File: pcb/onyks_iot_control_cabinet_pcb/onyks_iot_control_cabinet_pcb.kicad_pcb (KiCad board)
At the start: 2 copper layers, 80 x 90 mm, 38 parts, among them J1 Conn_01x02_Socket, J10 Conn_02x05_Odd_Even, J2 Conn_01x06_Socket, J3 Screw_Terminal_01x02, J4 Jack-DC, J5 Conn_01x03_Pin, J6 Conn_02x09_Odd_Even, J7 Screw_Terminal_01x02, J8 Conn_01x06_Pin, J9 Conn_01x02_Socket, Q1 SQ4050EY-T1_GE3, Q2 SQ4050EY-T1_GE3, Q3 NPN, Q4 NPN, SW1 SW_Push, SW2 SW_Push, SW3 SW_Push, U1 ESP32-WROOM-32D, U2 LMR51430

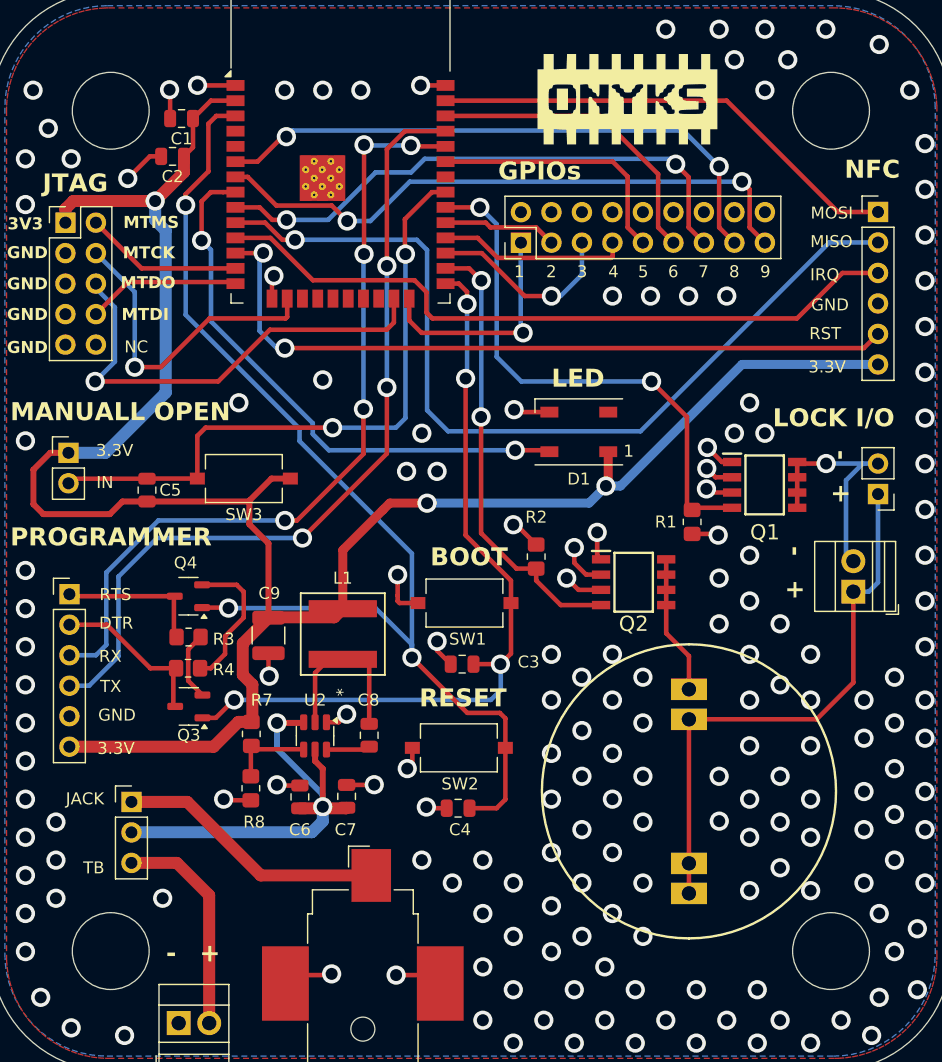
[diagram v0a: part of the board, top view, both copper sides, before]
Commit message: Karol can't add mounting holes/Added
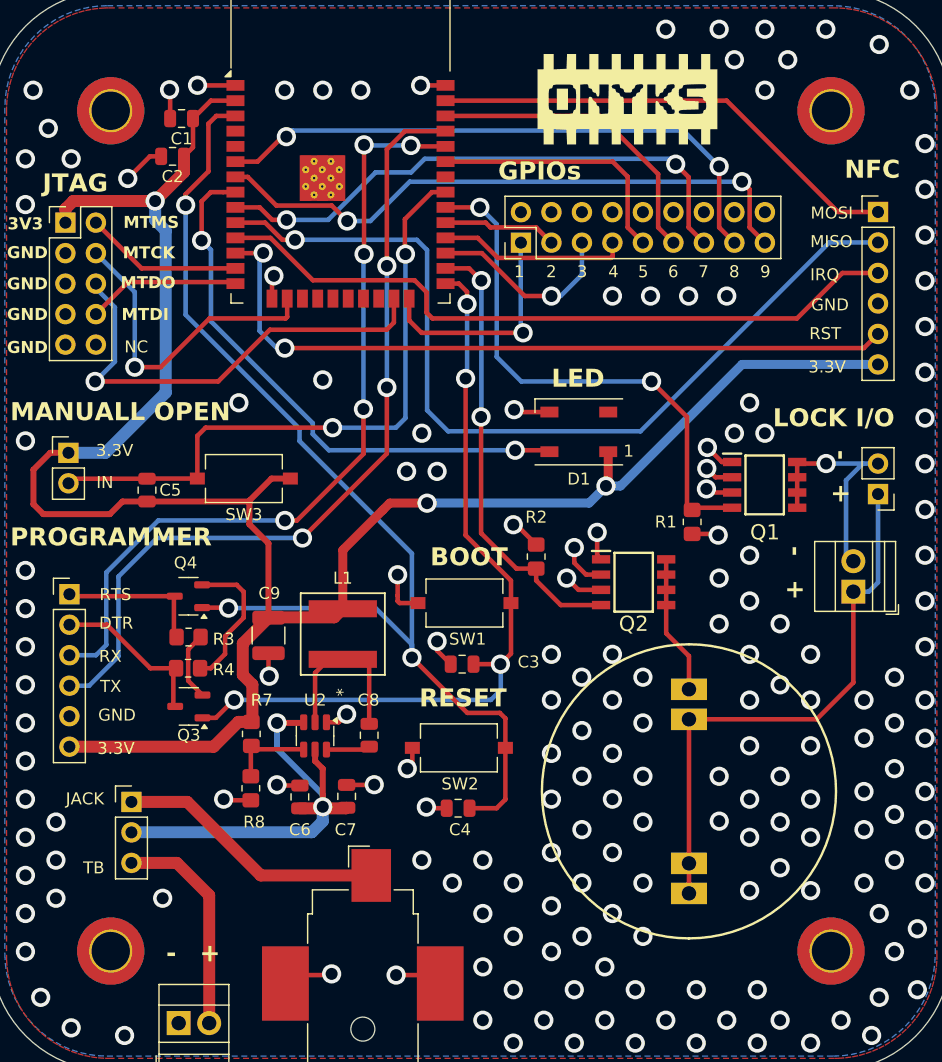
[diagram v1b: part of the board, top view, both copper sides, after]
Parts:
- added H1: MountingHole_Pad, MountingHole:MountingHole_3.2mm_M3_DIN965_Pad_TopBottom, F.Cu at (116.0, 36.0)
- added H2: MountingHole_Pad, MountingHole:MountingHole_3.2mm_M3_DIN965_Pad_TopBottom, F.Cu at (116.0, 106.0)
- added H3: MountingHole_Pad, MountingHole:MountingHole_3.2mm_M3_DIN965_Pad_TopBottom, F.Cu at (56.0, 36.0)
- added H4: MountingHole_Pad, MountingHole:MountingHole_3.2mm_M3_DIN965_Pad_TopBottom, F.Cu at (56.0, 106.0)
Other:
- outline, holes or cut-outs redrawn

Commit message: PCB Update for package
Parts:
- removed J9: Conn_01x02_Socket, Connector_PinHeader_2.54mm:PinHeader_1x02_P2.54mm_Vertical
- moved J3 25.3 mm to (87.0, 111.1)
- moved R2 10.2 mm to (101.6, 72.4)
- moved Q2 9.10 mm to (108.0, 71.8)
- moved R1 7.54 mm to (110.5, 65.8), turned to 90 degrees
- moved Q1 6.61 mm to (116.8, 65.4)
- moved J4 5.98 mm to (71.1, 104.4)
- moved J7 5.63 mm to (121.1, 80.6)
- moved BZ1 3.16 mm to (104.2, 83.5)
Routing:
- net GND: track 66.9 -> 37.2 mm, vias 180 -> 164
- net Net-(J3-Pin_2): track 18.2 -> 37.7 mm
- net LOCK_PLUS: track 46.8 -> 32.7 mm
- net BUZZER_SWITCH: track 37.5 -> 43.9 mm
- net Net-(J5-Pin_1): track 22.5 -> 16.2 mm
- net LOCK_MINUS: track 19.6 -> 15.3 mm, vias 1 -> 0
- net Net-(BZ1--_2): track 11.6 -> 15.0 mm
- net LOCK_SWITCH: track 45.1 -> 47.4 mm

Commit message: PCB Overhaul
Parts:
- removed C8: 0.1u, Capacitor_SMD:C_0805_2012Metric
- removed C9: 100u, Capacitor_SMD:C_1210_3225Metric
- removed G***: LOGO, ourFootprints:LOGO
- removed J8: Conn_01x06_Pin, Connector_PinHeader_2.54mm:PinHeader_1x06_P2.54mm_Vertical
- removed Q4: NPN, Package_TO_SOT_SMD:SOT-23-3
- removed R7: 100k, Resistor_SMD:R_0805_2012Metric_Pad1.20x1.40mm_HandSolder
- removed R8: 22.1k, Resistor_SMD:R_0805_2012Metric_Pad1.20x1.40mm_HandSolder
- added C10: 22u/10V, Capacitor_SMD:C_0603_1608Metric, F.Cu at (176.5, 53.3)
- added C11: 0.1u/50V, Capacitor_SMD:C_0603_1608Metric, F.Cu at (174.6, 53.3)
- added D2: S5J, Diode_SMD:D_SMC, F.Cu at (211.5, 82.5)
- added D3: S5J, Diode_SMD:D_SMC, F.Cu at (188.0, 100.6)
- added J9: Conn_02x05_Odd_Even, Connector_PinHeader_2.54mm:PinHeader_2x05_P2.54mm_Vertical, F.Cu at (164.1, 84.8)
- added Q5: PMV100ENEAR, Package_TO_SOT_SMD:SOT-23, F.Cu at (204.3, 82.9)
- added R5: 100k, Resistor_SMD:R_0805_2012Metric_Pad1.20x1.40mm_HandSolder, F.Cu at (180.8, 97.2)
- added R6: 22.1k, Resistor_SMD:R_0805_2012Metric_Pad1.20x1.40mm_HandSolder, F.Cu at (181.9, 92.5)
- BZ1: value Buzzer -> CPI2416100T
- C1: value 22u -> 0.1u/50V; footprint Capacitor_SMD:C_0805_2012Metric -> Capacitor_SMD:C_0603_1608Metric
- C2, C3: value 0.1u -> 0.1u/50V; footprint Capacitor_SMD:C_0805_2012Metric -> Capacitor_SMD:C_0603_1608Metric
- C4: value 0.1u -> 2.2u/50V; footprint Capacitor_SMD:C_0805_2012Metric -> Capacitor_SMD:C_0603_1608Metric
- C5: value 0.1u -> 100n/50V; footprint Capacitor_SMD:C_0805_2012Metric -> Capacitor_SMD:C_0603_1608Metric
- C6: value 2.2u -> 100n/50V
- C7: value 100n -> 100u/6.3V; footprint Capacitor_SMD:C_0805_2012Metric -> Capacitor_SMD:C_1210_3225Metric
- J1: value Conn_01x02_Socket -> Screw_Terminal_01x02; footprint Connector_PinHeader_2.54mm:PinHeader_1x02_P2.54mm_Vertical -> TerminalBlock:TerminalBlock_Xinya_XY308-2.54-2P_1x02_P2.54mm_Horizontal
- J10: value Conn_02x05_Odd_Even -> Conn_01x06_Pin; footprint Connector_PinHeader_2.54mm:PinHeader_2x05_P2.54mm_Vertical -> Connector_PinHeader_2.54mm:PinHeader_1x06_P2.54mm_Vertical
- J2: value Conn_01x06_Socket -> Screw_Terminal_01x02; footprint Connector_PinHeader_2.54mm:PinHeader_1x06_P2.54mm_Vertical -> TerminalBlock:TerminalBlock_Xinya_XY308-2.54-2P_1x02_P2.54mm_Horizontal
- J3: value Screw_Terminal_01x02 -> Jack-DC; footprint TerminalBlock:TerminalBlock_Xinya_XY308-2.54-2P_1x02_P2.54mm_Horizontal -> Connector_BarrelJack:BarrelJack_CUI_PJ-036AH-SMT_Horizontal
- J4: value Jack-DC -> Conn_01x03_Pin; footprint Connector_BarrelJack:BarrelJack_CUI_PJ-036AH-SMT_Horizontal -> Connector_PinHeader_2.54mm:PinHeader_1x03_P2.54mm_Vertical
- J5: value Conn_01x03_Pin -> Conn_02x09_Odd_Even; footprint Connector_PinHeader_2.54mm:PinHeader_1x03_P2.54mm_Vertical -> Connector_PinHeader_2.54mm:PinHeader_2x09_P2.54mm_Vertical
- J6: value Conn_02x09_Odd_Even -> Conn_01x06_Socket; footprint Connector_PinHeader_2.54mm:PinHeader_2x09_P2.54mm_Vertical -> Connector_PinHeader_2.54mm:PinHeader_1x06_P2.54mm_Vertical
- J7: value Screw_Terminal_01x02 -> Conn_01x02_Socket; footprint TerminalBlock:TerminalBlock_Xinya_XY308-2.54-2P_1x02_P2.54mm_Horizontal -> Connector_PinHeader_2.54mm:PinHeader_1x02_P2.54mm_Vertical
- L1: value 5.6u -> XAL6060-562MEC_COC
- Q1, Q2: value SQ4050EY-T1_GE3 -> NPN; footprint ourFootprints:SOIC127P600X175-8N -> Package_TO_SOT_SMD:SOT-23-3
- Q3: value NPN -> PMV100ENEAR; footprint Package_TO_SOT_SMD:SOT-23-3 -> Package_TO_SOT_SMD:SOT-23
- R1, R2: value 100 -> 10k
- R3, R4: value 10k -> 100
- U2: value LMR51430 -> LMR51430XDDCR
- moved H3 184.7 mm to (220.5, 120.1)
- moved J5 158.2 mm to (211.1, 54.9)
- moved J1 143.8 mm to (186.0, 118.1)
- moved R4 143.1 mm to (205.1, 93.4), turned to -90 degrees
- moved Q3 139.6 mm to (201.9, 93.4), turned to -90 degrees
- moved R3 138.8 mm to (201.2, 82.8), turned to 90 degrees
- moved J6 132.4 mm to (222.0, 59.4), turned to 0 degrees
- moved SW1 131.8 mm to (216.5, 90.8), turned to -90 degrees
- moved C3 127.1 mm to (212.1, 90.9), turned to -90 degrees
- moved C5 118.9 mm to (174.6, 95.2), turned to 180 degrees
- moved J10 117.7 mm to (161.5, 88.9), turned to 90 degrees
- moved U1 114.4 mm to (188.1, 60.4)
- moved C1 113.6 mm to (170.8, 69.0), turned to -90 degrees
- moved C7 111.9 mm to (187.5, 87.6), turned to -90 degrees
- moved J2 107.5 mm to (220.0, 83.8), turned to 90 degrees
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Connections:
- net Net-(D1-DIN) renamed /MCU/GPIO_32
- BZ1 pad A1: LOCK_PLUS -> +12V
- BZ1 pad B1: LOCK_PLUS -> +12V
- BZ1 pad B2: LOCK_PLUS -> +12V
- C1 pad 1: +3.3V -> /MCU/MCU_BOOT
- C2 pad 1: +3.3V -> /MCU/MCU_RESET
- C3 pad 1: GND -> +3.3V
- C3 pad 2: MCU_BOOT -> /MCU/GPIO_19
- C4 pad 1: GND -> +12V
- C4 pad 2: MCU_RESET -> GND
- C5 pad 1: +3.3V -> +12V
- C5 pad 2: LOCK_MCU_MANUAL_OPEN -> GND
- C6 pad 1: V_IN -> Net-(U2-CB)
- C6 pad 2: GND -> Net-(U2-SW)
- C7 pad 1: V_IN -> +3.3V
- J1 pad 1: +3.3V -> GND
- J1 pad 2: LOCK_MCU_MANUAL_OPEN -> Net-(J1-Pin_2)
- J10 pad 1: +3.3V -> /MCU/RTS
- J10 pad 2: JTAG_MTMS -> /MCU/DTR
- J10 pad 3: GND -> /MCU/RXD
- J10 pad 4: JTAG_MTCK -> /MCU/TXD
- J10 pad 6: JTAG_MTDO -> +3.3V
- J2 pad 1: NFC_MOSI -> +12V
- J2 pad 2: NFC_MISO -> Net-(D2-A)
- J3 pad 1: GND -> Net-(J4-Pin_1)
- J3 pad 2: Net-(J3-Pin_2) -> GND
- J4 pad 1: Net-(J5-Pin_1) -> Net-(J4-Pin_1)
- J4 pad 2: GND -> +12V
- J4 pad 3: GND -> Net-(J1-Pin_2)
- J5 pad 1: Net-(J5-Pin_1) -> /MCU/GPIO_2
- J5 pad 2: V_IN -> GND
- J5 pad 3: Net-(J3-Pin_2) -> /MCU/GPIO_5
- J6 pad 1: FREE_GPIO_1 -> /MCU/GPIO_23
- J6 pad 2: GND -> /MCU/GPIO_25
- J6 pad 3: FREE_GPIO_2 -> /MCU/GPIO_26
- J6 pad 5: FREE_GPIO_3 -> /MCU/GPIO_27
- J6 pad 6: GND -> +3.3V
- J7 pad 1: LOCK_PLUS -> +3.3V
- J7 pad 2: LOCK_MINUS -> /MCU/GPIO_19
- Q1 pad 1: GND -> /MCU/MCU_BOOT
- Q1 pad 2: GND -> Net-(Q1-B)
- Q1 pad 3: GND -> /MCU/DTR
- Q2 pad 1: GND -> /MCU/MCU_RESET
- Q2 pad 2: GND -> Net-(Q2-B)
- Q2 pad 3: GND -> /MCU/RTS
- Q3 pad 1: MCU_BOOT -> /MCU/GPIO_4
- Q3 pad 2: Net-(Q3-B) -> GND
- Q3 pad 3: DTR -> Net-(BZ1--_2)
- R1 pad 1: LOCK_SWITCH -> Net-(Q1-B)
- R1 pad 2: GND -> /MCU/RTS
- R2 pad 1: BUZZER_SWITCH -> Net-(Q2-B)
- R2 pad 2: GND -> /MCU/DTR
- R3 pad 1: Net-(Q3-B) -> /MCU/GPIO_18
- R3 pad 2: RTS -> GND
- R4 pad 1: Net-(Q4-B) -> /MCU/GPIO_4
- R4 pad 2: DTR -> GND
- SW1 pad 1: GND -> +3.3V
- SW1 pad 2: MCU_BOOT -> /MCU/GPIO_19
- SW2 pad 1: GND -> /MCU/MCU_BOOT
- SW2 pad 2: MCU_RESET -> GND
- SW3 pad 1: +3.3V -> /MCU/MCU_RESET
- SW3 pad 2: LOCK_MCU_MANUAL_OPEN -> GND
- U1 pad 10: NFC_MISO -> /MCU/GPIO_25
- U1 pad 11: NFC_IRQ -> /MCU/GPIO_26
- U1 pad 12: NFC_RST -> /MCU/GPIO_27
- U1 pad 13: JTAG_MTMS -> /MCU/MTMS
- U1 pad 14: JTAG_MTDI -> /MCU/MTDI
- U1 pad 16: JTAG_MTCK -> /MCU/MTCK
- U1 pad 23: JTAG_MTDO -> /MCU/MTDO
- U1 pad 24: FREE_GPIO_1 -> /MCU/GPIO_2
- U1 pad 25: MCU_BOOT -> /MCU/MCU_BOOT
- U1 pad 26: BUZZER_SWITCH -> /MCU/GPIO_4
- U1 pad 27: FREE_GPIO_3 -> /MCU/GPIO_16
- U1 pad 28: FREE_GPIO_4 -> /MCU/GPIO_17
- U1 pad 29: FREE_GPIO_2 -> /MCU/GPIO_5
- U1 pad 3: MCU_RESET -> /MCU/MCU_RESET
- U1 pad 30: LOCK_SWITCH -> /MCU/GPIO_18
- U1 pad 31: LOCK_MCU_MANUAL_OPEN -> /MCU/GPIO_19
- U1 pad 33: FREE_GPIO_5 -> /MCU/GPIO_21
- U1 pad 34: MCU_RX_PROG -> /MCU/RXD
- U1 pad 35: MCU_TX_PROG -> /MCU/TXD
- U1 pad 36: FREE_GPIO_6 -> /MCU/GPIO_22
- U1 pad 37: NFC_MOSI -> /MCU/GPIO_23
- U1 pad 6: FREE_GPIO_8 -> /MCU/GPIO_34
- U1 pad 7: FREE_GPIO_9 -> /MCU/GPIO_35
- U1 pad 9: FREE_GPIO_7 -> /MCU/GPIO_33
- U2 pad 3: V_IN -> +12V
- U2 pad 5: V_IN -> +12V
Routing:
- net MCU_RESET: track 95.5 -> 0.00 mm, vias 3 -> 0
- net /MCU/GPIO_25: track 0.00 -> 77.0 mm, vias 0 -> 1
- net /MCU/GPIO_26: track 0.00 -> 75.6 mm, vias 0 -> 1
- net NFC_MISO: track 75.1 -> 0.00 mm, vias 1 -> 0
- net /MCU/RXD: track 0.00 -> 73.9 mm, vias 0 -> 1
- net /MCU/GPIO_27: track 0.00 -> 69.6 mm, vias 0 -> 1
- net MCU_TX_PROG: track 69.2 -> 0.00 mm, vias 3 -> 0
- net /MCU/TXD: track 0.00 -> 68.9 mm, vias 0 -> 1
- net MCU_RX_PROG: track 67.6 -> 0.00 mm, vias 5 -> 0
- net MCU_BOOT: track 65.3 -> 0.00 mm, vias 4 -> 0
- net /MCU/GPIO_19: track 0.00 -> 63.4 mm, vias 0 -> 2
- net NFC_RST: track 61.5 -> 0.00 mm, vias 2 -> 0
- net /MCU/MCU_BOOT: track 0.00 -> 60.6 mm, vias 0 -> 2
- net /MCU/GPIO_33: track 0.00 -> 60.5 mm, vias 0 -> 3
- net /MCU/GPIO_35: track 0.00 -> 58.9 mm, vias 0 -> 2
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- added copper zone on B.Cu, net +12V
- added copper zone on B.Cu, net Net-(J1-Pin_2)
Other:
- board size 80 x 90 mm -> 68.3 x 79.2 mm
- board text removed: "+"
- board text removed: "-"
- board text removed: "1"
- board text removed: "2"
- board text removed: "3"
- board text removed: "3.3V"
- board text removed: "3V3"
- board text removed: "4"
- board text removed: "5"
- board text removed: "6"
- board text removed: "7"
- board text removed: "8"
- board text removed: "9"
- board text removed: "BOOT"
- board text removed: "DTR"
- board text removed: "GND"
- board text removed: "GPIOs"
- board text removed: "IN"
- board text removed: "IRQ"
- board text removed: "JACK"
- board text removed: "JTAG"
- board text removed: "LED"
- board text removed: "LOCK I/O"
- board text removed: "MANUALL OPEN"
- board text removed: "MISO"
- board text removed: "MOSI"
- board text removed: "MTCK"
- board text removed: "MTDI"
- board text removed: "MTDO"
- board text removed: "MTMS"
- board text removed: "NC"
- board text removed: "NFC"
- board text removed: "PROGRAMMER"
- board text removed: "RESET"
- board text removed: "RST"
- board text removed: "RTS"
- board text removed: "RX"
- board text removed: "TB"
- board text removed: "TX"

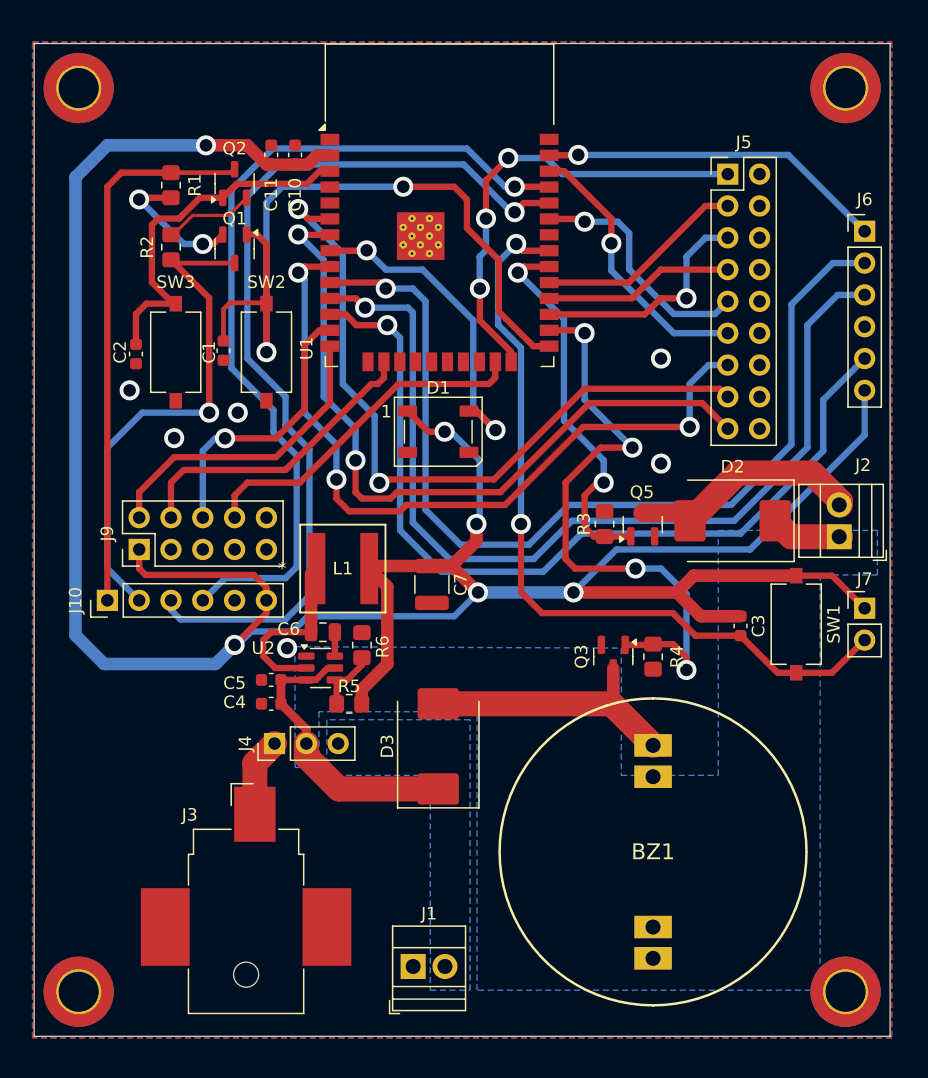
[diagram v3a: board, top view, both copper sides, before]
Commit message: Round corners and the logo
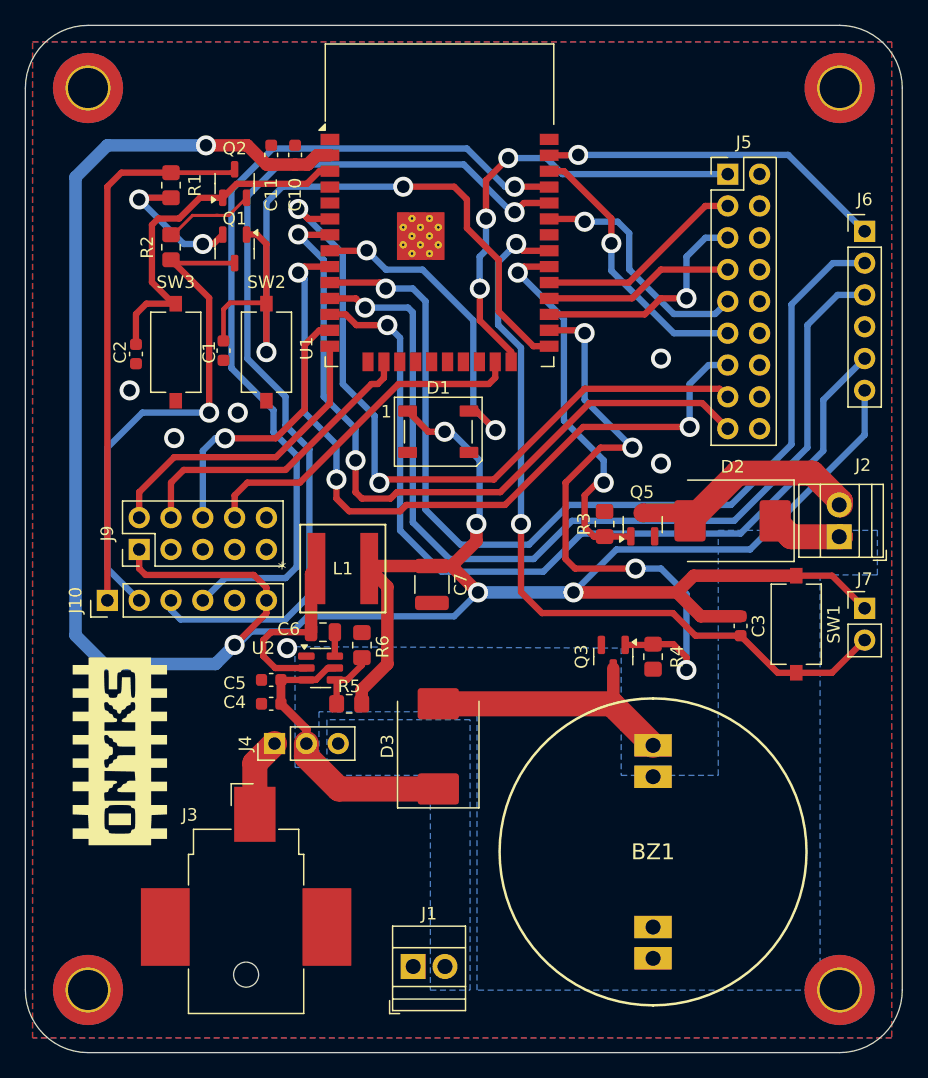
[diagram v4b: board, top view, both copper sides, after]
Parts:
- added G***: LOGO, ourFootprints:LOGO, F.Cu at (162.5, 101.0)
- moved H4 0.76 mm to (160.0, 120.0)
- moved H2 0.74 mm to (160.0, 48.0)
- moved H3 0.49 mm to (220.0, 120.0)
- moved H1 0.47 mm to (220.0, 48.0)
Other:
- board size 68.3 x 79.2 mm -> 70 x 82 mm

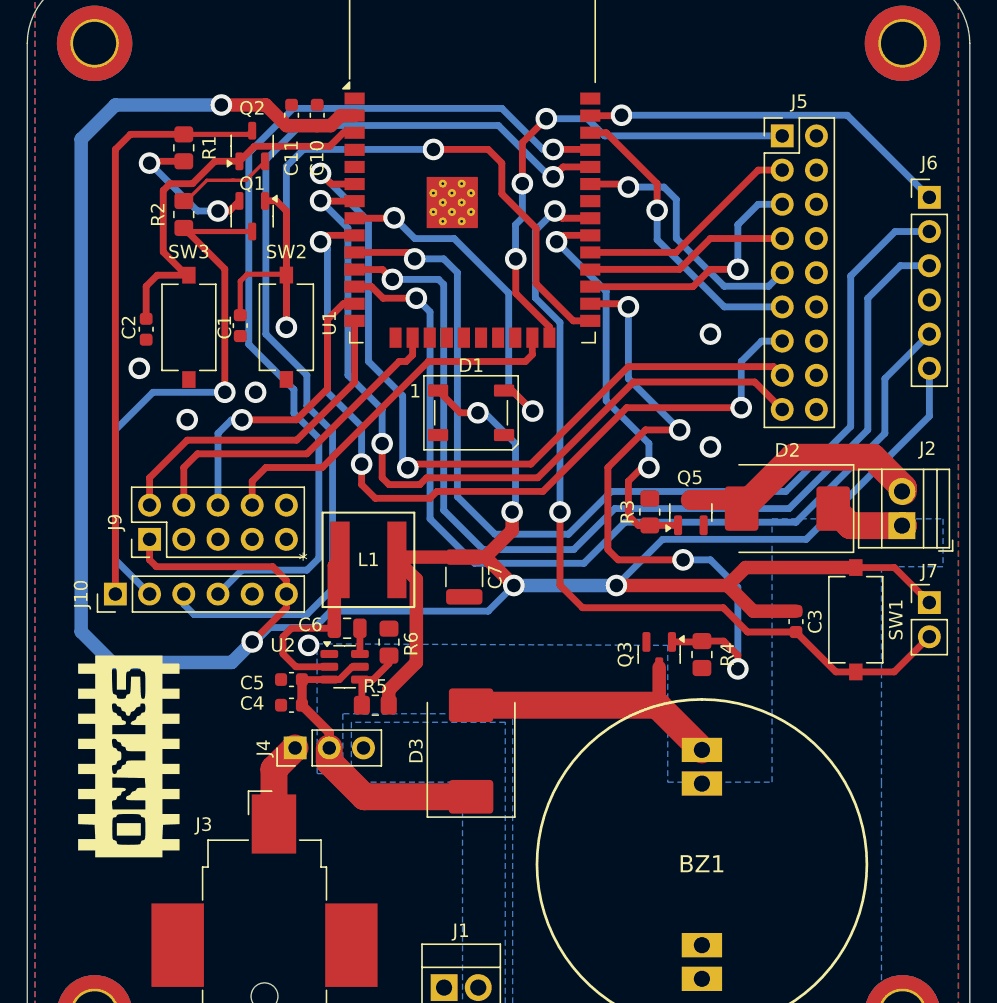
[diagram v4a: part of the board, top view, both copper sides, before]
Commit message: Add descriptions to ports
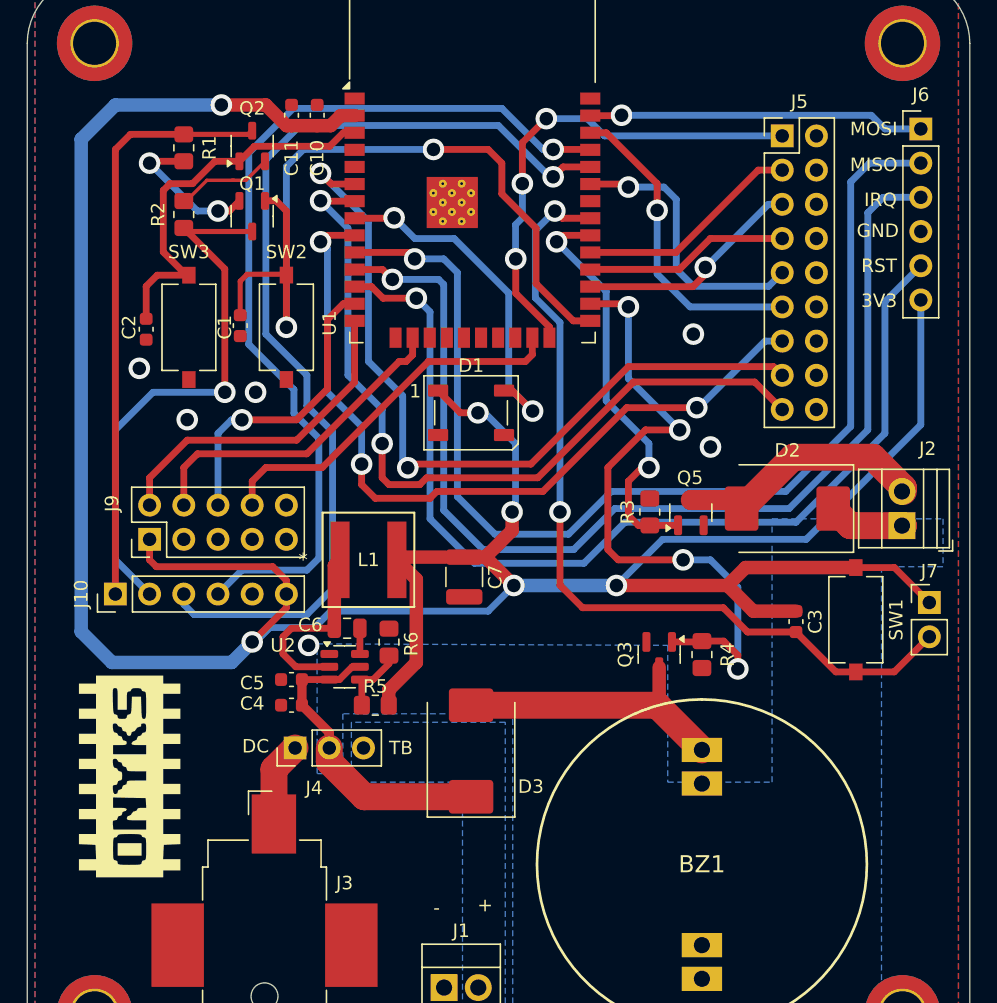
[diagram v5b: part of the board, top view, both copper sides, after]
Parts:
- moved J6 5.12 mm to (221.4, 54.4)
- moved G*** 1.49 mm to (162.6, 102.5)
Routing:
- net /MCU/GPIO_25: track 77.0 -> 82.5 mm
- net /MCU/GPIO_26: track 75.6 -> 80.8 mm
- net +3.3V: track 220.1 -> 224.9 mm
- net /MCU/GPIO_27: track 69.6 -> 74.4 mm
- net /MCU/GPIO_23: track 27.7 -> 25.0 mm
- net /MCU/GPIO_33: track 60.5 -> 58.5 mm
- net /MCU/GPIO_22: track 22.1 -> 23.5 mm
- net /MCU/GPIO_21: track 19.5 -> 20.9 mm
- net /MCU/GPIO_16: track 18.7 -> 17.5 mm
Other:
- board text added: "+"
- board text added: "-"
- board text added: "16"
- board text added: "17"
- board text added: "2"
- board text added: "21"
- board text added: "22"
- board text added: "33"
- board text added: "34"
- board text added: "35"
- board text added: "3V3"
- board text added: "5"
- board text added: "DC"
- board text added: "DTR"
- board text added: "GND"
- board text added: "IRQ"
- board text added: "MISO"
- board text added: "MOSI"
- board text added: "MTCK"
- board text added: "MTDI"
- board text added: "MTDO"
- board text added: "MTMS"
- board text added: "RST"
- board text added: "RTS"
- board text added: "RXD"
- board text added: "TB"
- board text added: "TXD"
